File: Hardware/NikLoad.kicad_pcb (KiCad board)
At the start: 2 copper layers, 9 parts, among them Q500 IRFZ24NPbF, Q501 IRFZ24NPbF, Q502 IRFZ24NPbF, Q503 IRFZ24NPbF, Q504 IRFZ24NPbF, Q505 IRFZ24NPbF, Q506 IRFZ24NPbF, Q507 IRFZ24NPbF

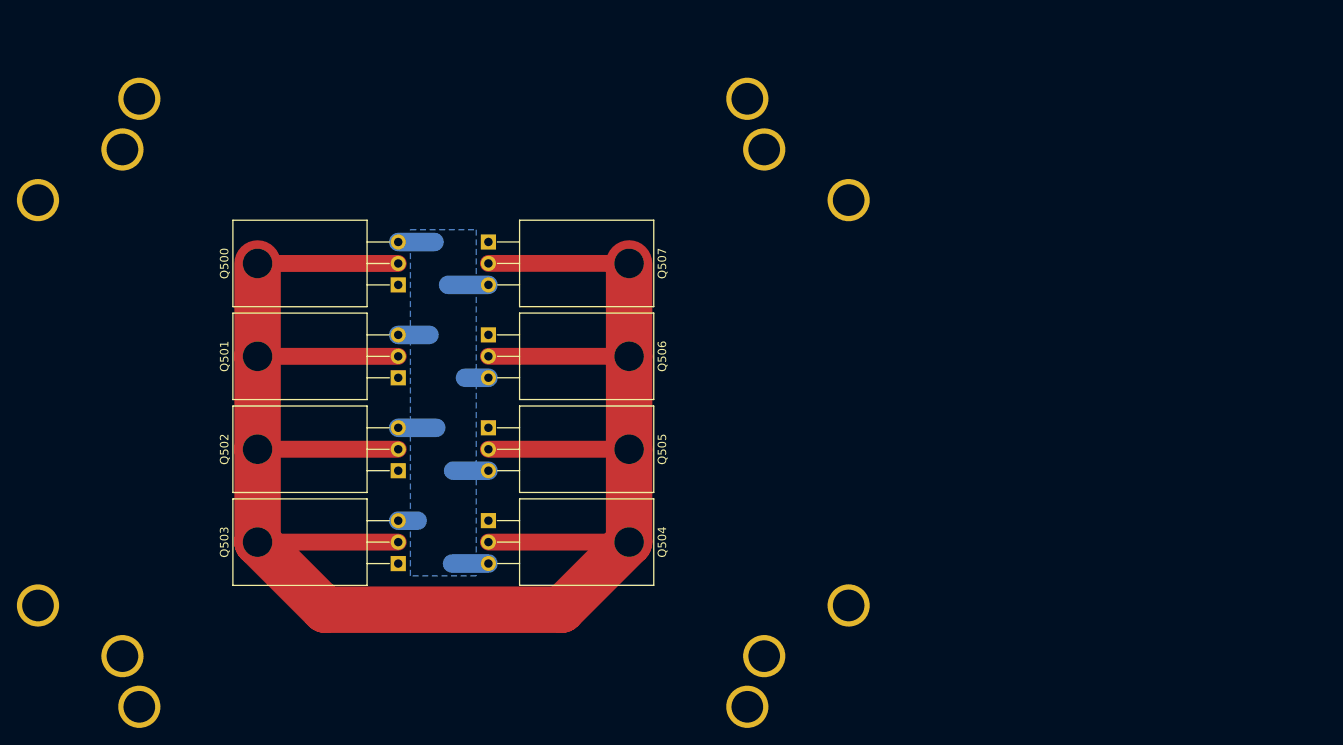
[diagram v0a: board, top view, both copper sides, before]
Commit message: Add current sense
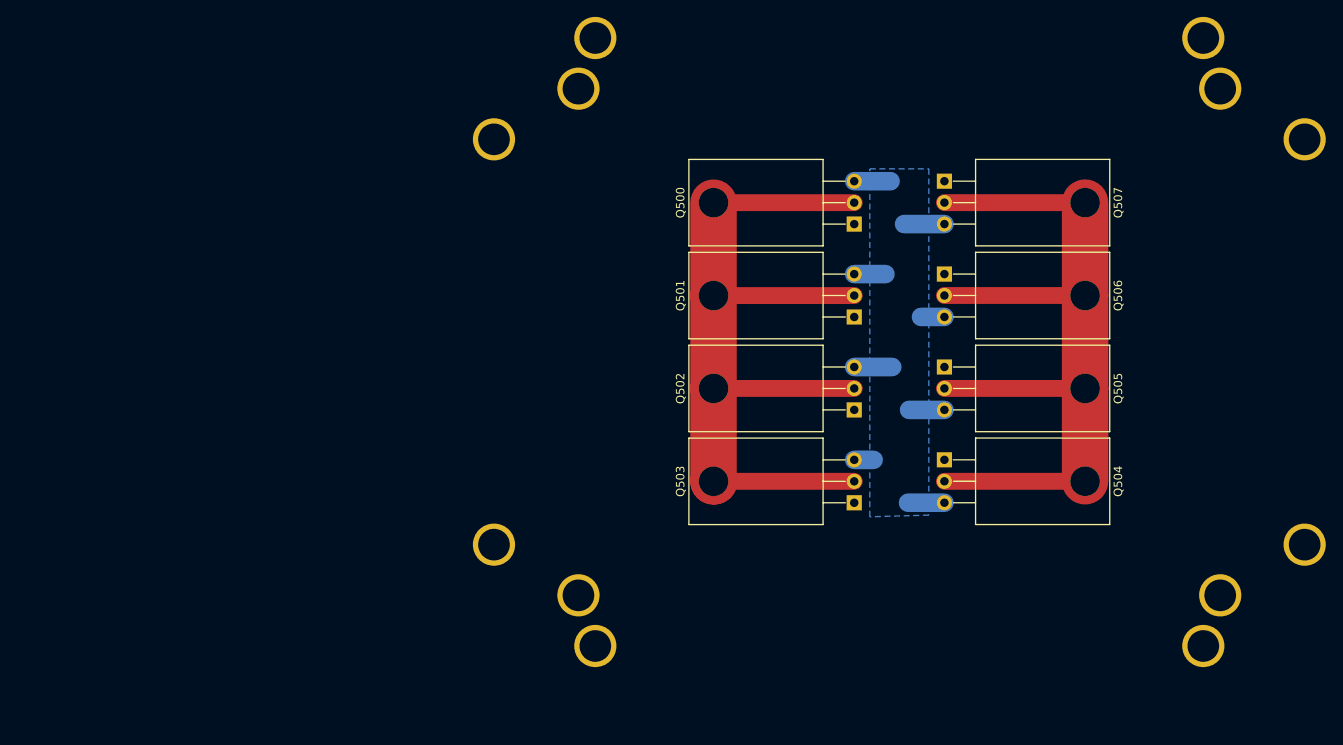
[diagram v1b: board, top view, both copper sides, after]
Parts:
- moved Q500 54.5 mm to (184.2, 77.3)
- moved Q501 54.5 mm to (184.2, 88.3)
- moved Q502 54.5 mm to (184.2, 99.3)
- moved Q503 54.5 mm to (184.2, 110.3)
- moved Q504 54.5 mm to (194.8, 105.3)
- moved Q506 54.5 mm to (194.8, 83.3)
- moved Q507 54.5 mm to (194.8, 72.3)
- moved REF** 54.5 mm to (189.5, 91.3)
- moved Q505 54.5 mm to (194.8, 94.3)
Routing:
- net DUT+: track 250.0 -> 199.4 mm
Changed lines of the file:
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@@
 (kicad_pcb (version 4) (host pcbnew 4.0.7)
   (general
-    (links 22)
-    (no_connects 7)
-    (area 84.8476 59.0726 186.1524 137.1524)
+    (links 0)
+    (no_connects 1)
+    (area 138.8476 51.8726 240.1524 129.9524)
     (thickness 1.6)
     (drawings 0)
-    (tracks 26)
+    (tracks 23)
     (zones 0)
     (modules 9)
@@
   )
   (module pc_cooler_mount:PC_COOLER_MOUNT (layer F.Cu)
-    (at 135.5 98.5)
+    (at 189.5 91.3)
     (fp_text reference REF** (at 19.5 -38.5) (layer F.SilkS) hide
       (effects (font (size 1 1) (thickness 0.15)))
@@
   )
   (module TO-220_plated_mount:TO-220_Horizontal (layer F.Cu)
-    (at 130.16 84.54 90)
+    (at 184.16 77.34 90)
     (descr "TO-220, Horizontal, RM 2.54mm")
     (tags "TO-220 Horizontal RM 2.54mm")
@@
   )
   (module TO-220_plated_mount:TO-220_Horizontal (layer F.Cu)
-    (at 130.16 95.54 90)
+    (at 184.16 88.34 90)
     (descr "TO-220, Horizontal, RM 2.54mm")
     (tags "TO-220 Horizontal RM 2.54mm")
@@
   )
   (module TO-220_plated_mount:TO-220_Horizontal (layer F.Cu)
-    (at 130.16 106.54 90)
+    (at 184.16 99.34 90)
     (descr "TO-220, Horizontal, RM 2.54mm")
     (tags "TO-220 Horizontal RM 2.54mm")
@@
   )
   (module TO-220_plated_mount:TO-220_Horizontal (layer F.Cu)
-    (at 130.16 117.54 90)
+    (at 184.16 110.34 90)
     (descr "TO-220, Horizontal, RM 2.54mm")
     (tags "TO-220 Horizontal RM 2.54mm")
@@
   )
   (module TO-220_plated_mount:TO-220_Horizontal (layer F.Cu)
-    (at 140.84 112.455 270)
+    (at 194.84 105.255 270)
     (descr "TO-220, Horizontal, RM 2.54mm")
     (tags "TO-220 Horizontal RM 2.54mm")
@@
   )
   (module TO-220_plated_mount:TO-220_Horizontal (layer F.Cu)
-    (at 140.84 101.46 270)
+    (at 194.84 94.26 270)
     (descr "TO-220, Horizontal, RM 2.54mm")
     (tags "TO-220 Horizontal RM 2.54mm")
@@
   )
   (module TO-220_plated_mount:TO-220_Horizontal (layer F.Cu)
-    (at 140.84 90.455 270)
+    (at 194.84 83.255 270)
     (descr "TO-220, Horizontal, RM 2.54mm")
     (tags "TO-220 Horizontal RM 2.54mm")
@@
   )
   (module TO-220_plated_mount:TO-220_Horizontal (layer F.Cu)
-    (at 140.84 79.455 270)
+    (at 194.84 72.255 270)
     (descr "TO-220, Horizontal, RM 2.54mm")
     (tags "TO-220 Horizontal RM 2.54mm")
@@
     )
   )
-  (segment (start 149.495 123) (end 121.5 123) (width 5.5) (layer F.Cu) (net 9))
-  (segment (start 121.5 123) (end 113.5 115) (width 5.5) (layer F.Cu) (net 9))
-  (segment (start 149.495 123) (end 157.5 114.995) (width 5.5) (layer F.Cu) (net 9))
-  (segment (start 113.6 115) (end 113.5 115) (width 5.5) (layer F.Cu) (net 9))
-  (segment (start 157.5 92.995) (end 157.5 81.995) (width 5.5) (layer F.Cu) (net 9))
-  (segment (start 157.5 104) (end 157.5 92.995) (width 5.5) (layer F.Cu) (net 9))
-  (segment (start 157.5 114.995) (end 157.5 104) (width 5.5) (layer F.Cu) (net 9))
-  (segment (start 113.5 104) (end 113.5 115) (width 5.5) (layer F.Cu) (net 9))
-  (segment (start 113.5 93) (end 113.5 104) (width 5.5) (layer F.Cu) (net 9))
-  (segment (start 113.5 82) (end 113.5 93) (width 5.5) (layer F.Cu) (net 9))
-  (segment (start 140.84 81.995) (end 157.5 81.995) (width 2) (layer F.Cu) (net 9))
-  (segment (start 140.84 92.995) (end 157.5 92.995) (width 2) (layer F.Cu) (net 9))
-  (segment (start 140.84 104) (end 157.5 104) (width 2) (layer F.Cu) (net 9))
-  (segment (start 140.84 114.995) (end 157.5 114.995) (width 2) (layer F.Cu) (net 9))
-  (segment (start 130.16 115) (end 113.5 115) (width 2) (layer F.Cu) (net 9))
-  (segment (start 130.16 104) (end 113.5 104) (width 2) (layer F.Cu) (net 9))
-  (segment (start 130.16 93) (end 113.5 93) (width 2) (layer F.Cu) (net 9))
-  (segment (start 130.16 82) (end 113.5 82) (width 2) (layer F.Cu) (net 9))
-  (segment (start 140.84 117.535) (end 136.535 117.535) (width 2.2) (layer B.Cu) (net 10))
-  (segment (start 130.16 112.46) (end 132.46 112.46) (width 2.2) (layer B.Cu) (net 10))
-  (segment (start 140.84 106.54) (end 136.66 106.54) (width 2.2) (layer B.Cu) (net 10))
-  (segment (start 130.16 101.46) (end 134.66 101.46) (width 2.2) (layer B.Cu) (net 10))
-  (segment (start 140.84 95.535) (end 138.065 95.535) (width 2.2) (layer B.Cu) (net 10))
-  (segment (start 130.16 90.46) (end 133.86 90.46) (width 2.2) (layer B.Cu) (net 10))
-  (segment (start 140.84 84.535) (end 136.065 84.535) (width 2.2) (layer B.Cu) (net 10))
-  (segment (start 130.16 79.46) (end 134.46 79.46) (width 2.2) (layer B.Cu) (net 10))
+  (segment (start 167.6 107.8) (end 167.5 107.8) (width 5.5) (layer F.Cu) (net 9))
+  (segment (start 211.5 85.795) (end 211.5 74.795) (width 5.5) (layer F.Cu) (net 9))
+  (segment (start 211.5 96.8) (end 211.5 85.795) (width 5.5) (layer F.Cu) (net 9))
+  (segment (start 211.5 107.795) (end 211.5 96.8) (width 5.5) (layer F.Cu) (net 9))
+  (segment (start 167.5 96.8) (end 167.5 107.8) (width 5.5) (layer F.Cu) (net 9))
+  (segment (start 167.5 85.8) (end 167.5 96.8) (width 5.5) (layer F.Cu) (net 9))
+  (segment (start 167.5 74.8) (end 167.5 85.8) (width 5.5) (layer F.Cu) (net 9))
+  (segment (start 194.84 74.795) (end 211.5 74.795) (width 2) (layer F.Cu) (net 9))
+  (segment (start 194.84 85.795) (end 211.5 85.795) (width 2) (layer F.Cu) (net 9))
+  (segment (start 194.84 96.8) (end 211.5 96.8) (width 2) (layer F.Cu) (net 9))
+  (segment (start 194.84 107.795) (end 211.5 107.795) (width 2) (layer F.Cu) (net 9))
+  (segment (start 184.16 107.8) (end 167.5 107.8) (width 2) (layer F.Cu) (net 9))
+  (segment (start 184.16 96.8) (end 167.5 96.8) (width 2) (layer F.Cu) (net 9))
+  (segment (start 184.16 85.8) (end 167.5 85.8) (width 2) (layer F.Cu) (net 9))
+  (segment (start 184.16 74.8) (end 167.5 74.8) (width 2) (layer F.Cu) (net 9))
+  (segment (start 194.84 110.335) (end 190.535 110.335) (width 2.2) (layer B.Cu) (net 10))
+  (segment (start 184.16 105.26) (end 186.46 105.26) (width 2.2) (layer B.Cu) (net 10))
+  (segment (start 194.84 99.34) (end 190.66 99.34) (width 2.2) (layer B.Cu) (net 10))
+  (segment (start 184.16 94.26) (end 188.66 94.26) (width 2.2) (layer B.Cu) (net 10))
+  (segment (start 194.84 88.335) (end 192.065 88.335) (width 2.2) (layer B.Cu) (net 10))
+  (segment (start 184.16 83.26) (end 187.86 83.26) (width 2.2) (layer B.Cu) (net 10))
+  (segment (start 194.84 77.335) (end 190.065 77.335) (width 2.2) (layer B.Cu) (net 10))
+  (segment (start 184.16 72.26) (end 188.46 72.26) (width 2.2) (layer B.Cu) (net 10))
   (zone (net 10) (net_name CURRENT_SENSE+) (layer B.Cu) (hatch edge 0.508)
     (priority 10)
@@
     (polygon
       (pts
-        (xy 131.6 78) (xy 139.4 78) (xy 139.4 119) (xy 131.6 119)
+        (xy 186 70.8) (xy 193 70.8) (xy 193 111.8) (xy 186 112)
       )
     )
   )
-  (zone (net 10) (net_name CURRENT_SENSE+) (layer F.Mask) (hatch edge 0.508)
+  (zone (net 0) (net_name "") (layer F.Mask) (hatch edge 0.508)
     (priority 10)
     (connect_pads (clearance 0.508))
@@
     (polygon
       (pts
-        (xy 116.2 117.4) (xy 116.2 79.2) (xy 110.6 79.2) (xy 110.6 117.4)
+        (xy 170.2 110.2) (xy 170.2 72) (xy 164.6 72) (xy 164.6 110.2)
       )
     )
   )
-  (zone (net 10) (net_name CURRENT_SENSE+) (layer F.Mask) (hatch edge 0.508)
+  (zone (net 0) (net_name "") (layer F.Mask) (hatch edge 0.508)
     (priority 10)
     (connect_pads (clearance 0.508))
@@
     (polygon
       (pts
-        (xy 160.322941 117.4) (xy 160.322941 79.2) (xy 154.722941 79.2) (xy 154.722941 117.4)
+        (xy 214.322941 110.2) (xy 214.322941 72) (xy 208.722941 72) (xy 208.722941 110.2)
       )
     )

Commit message: Preliminary measurement setup
Deleted net file, not yet needed.
Added preliminary measurement stuff.
Still need DAC for the offset voltage, and need to find a new ADC.
Also, doing isolation. Analog board will have +12V in, isolate power on board.
Isolated 2 channels of SPI between digital and analog.
Also, add a bunch of files I forgot to add to git. Oops.
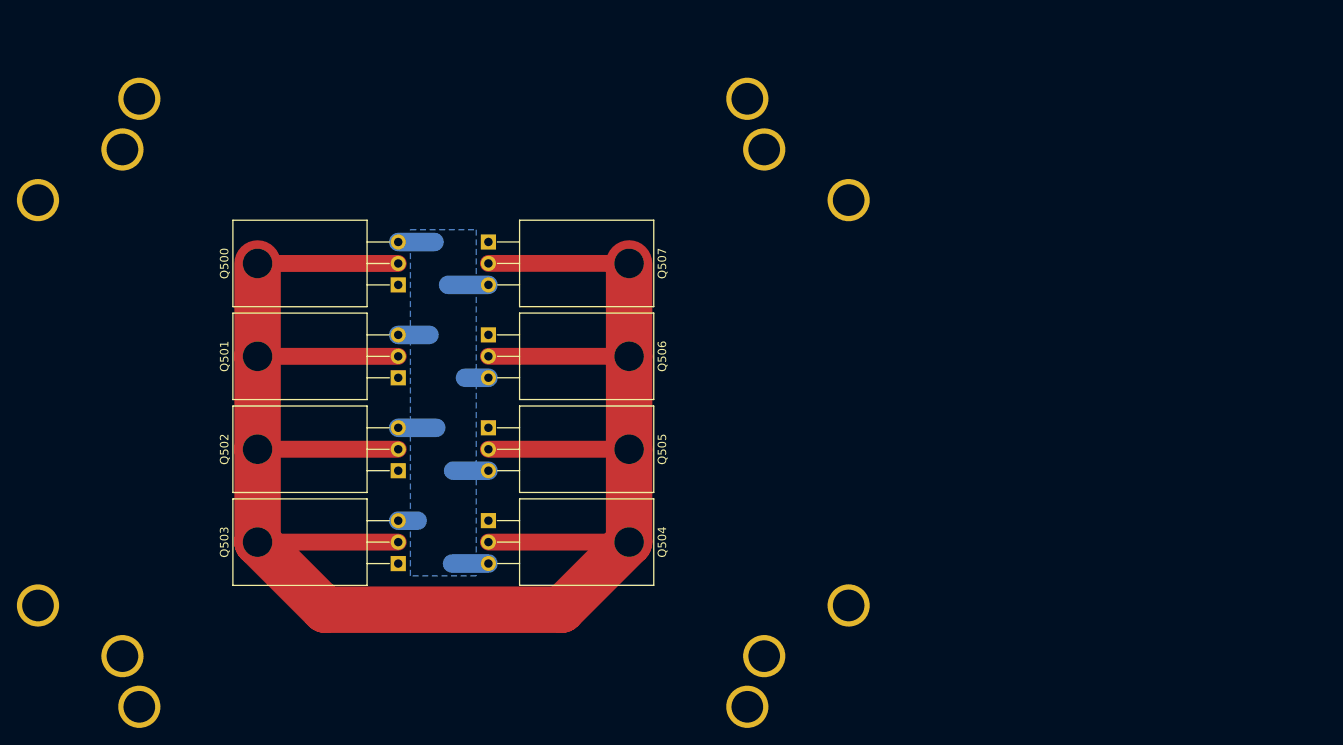
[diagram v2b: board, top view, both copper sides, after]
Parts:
- moved Q500 54.5 mm to (130.2, 84.5)
- moved Q501 54.5 mm to (130.2, 95.5)
- moved Q502 54.5 mm to (130.2, 106.5)
- moved Q503 54.5 mm to (130.2, 117.5)
- moved Q504 54.5 mm to (140.8, 112.5)
- moved Q506 54.5 mm to (140.8, 90.5)
- moved Q507 54.5 mm to (140.8, 79.5)
- moved REF** 54.5 mm to (135.5, 98.5)
- moved Q505 54.5 mm to (140.8, 101.5)
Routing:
- net DUT+: track 199.4 -> 250.0 mm
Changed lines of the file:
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@@
 (kicad_pcb (version 4) (host pcbnew 4.0.7)
   (general
-    (links 0)
-    (no_connects 1)
-    (area 138.8476 51.8726 240.1524 129.9524)
+    (links 22)
+    (no_connects 7)
+    (area 84.8476 59.0726 186.1524 137.1524)
     (thickness 1.6)
     (drawings 0)
-    (tracks 23)
+    (tracks 26)
     (zones 0)
     (modules 9)
@@
   )
   (module pc_cooler_mount:PC_COOLER_MOUNT (layer F.Cu)
-    (at 189.5 91.3)
+    (at 135.5 98.5)
     (fp_text reference REF** (at 19.5 -38.5) (layer F.SilkS) hide
       (effects (font (size 1 1) (thickness 0.15)))
@@
   )
   (module TO-220_plated_mount:TO-220_Horizontal (layer F.Cu)
-    (at 184.16 77.34 90)
+    (at 130.16 84.54 90)
     (descr "TO-220, Horizontal, RM 2.54mm")
     (tags "TO-220 Horizontal RM 2.54mm")
@@
   )
   (module TO-220_plated_mount:TO-220_Horizontal (layer F.Cu)
-    (at 184.16 88.34 90)
+    (at 130.16 95.54 90)
     (descr "TO-220, Horizontal, RM 2.54mm")
     (tags "TO-220 Horizontal RM 2.54mm")
@@
   )
   (module TO-220_plated_mount:TO-220_Horizontal (layer F.Cu)
-    (at 184.16 99.34 90)
+    (at 130.16 106.54 90)
     (descr "TO-220, Horizontal, RM 2.54mm")
     (tags "TO-220 Horizontal RM 2.54mm")
@@
   )
   (module TO-220_plated_mount:TO-220_Horizontal (layer F.Cu)
-    (at 184.16 110.34 90)
+    (at 130.16 117.54 90)
     (descr "TO-220, Horizontal, RM 2.54mm")
     (tags "TO-220 Horizontal RM 2.54mm")
@@
   )
   (module TO-220_plated_mount:TO-220_Horizontal (layer F.Cu)
-    (at 194.84 105.255 270)
+    (at 140.84 112.455 270)
     (descr "TO-220, Horizontal, RM 2.54mm")
     (tags "TO-220 Horizontal RM 2.54mm")
@@
   )
   (module TO-220_plated_mount:TO-220_Horizontal (layer F.Cu)
-    (at 194.84 94.26 270)
+    (at 140.84 101.46 270)
     (descr "TO-220, Horizontal, RM 2.54mm")
     (tags "TO-220 Horizontal RM 2.54mm")
@@
   )
   (module TO-220_plated_mount:TO-220_Horizontal (layer F.Cu)
-    (at 194.84 83.255 270)
+    (at 140.84 90.455 270)
     (descr "TO-220, Horizontal, RM 2.54mm")
     (tags "TO-220 Horizontal RM 2.54mm")
@@
   )
   (module TO-220_plated_mount:TO-220_Horizontal (layer F.Cu)
-    (at 194.84 72.255 270)
+    (at 140.84 79.455 270)
     (descr "TO-220, Horizontal, RM 2.54mm")
     (tags "TO-220 Horizontal RM 2.54mm")
@@
     )
   )
-  (segment (start 167.6 107.8) (end 167.5 107.8) (width 5.5) (layer F.Cu) (net 9))
-  (segment (start 211.5 85.795) (end 211.5 74.795) (width 5.5) (layer F.Cu) (net 9))
-  (segment (start 211.5 96.8) (end 211.5 85.795) (width 5.5) (layer F.Cu) (net 9))
-  (segment (start 211.5 107.795) (end 211.5 96.8) (width 5.5) (layer F.Cu) (net 9))
-  (segment (start 167.5 96.8) (end 167.5 107.8) (width 5.5) (layer F.Cu) (net 9))
-  (segment (start 167.5 85.8) (end 167.5 96.8) (width 5.5) (layer F.Cu) (net 9))
-  (segment (start 167.5 74.8) (end 167.5 85.8) (width 5.5) (layer F.Cu) (net 9))
-  (segment (start 194.84 74.795) (end 211.5 74.795) (width 2) (layer F.Cu) (net 9))
-  (segment (start 194.84 85.795) (end 211.5 85.795) (width 2) (layer F.Cu) (net 9))
-  (segment (start 194.84 96.8) (end 211.5 96.8) (width 2) (layer F.Cu) (net 9))
-  (segment (start 194.84 107.795) (end 211.5 107.795) (width 2) (layer F.Cu) (net 9))
-  (segment (start 184.16 107.8) (end 167.5 107.8) (width 2) (layer F.Cu) (net 9))
-  (segment (start 184.16 96.8) (end 167.5 96.8) (width 2) (layer F.Cu) (net 9))
-  (segment (start 184.16 85.8) (end 167.5 85.8) (width 2) (layer F.Cu) (net 9))
-  (segment (start 184.16 74.8) (end 167.5 74.8) (width 2) (layer F.Cu) (net 9))
-  (segment (start 194.84 110.335) (end 190.535 110.335) (width 2.2) (layer B.Cu) (net 10))
-  (segment (start 184.16 105.26) (end 186.46 105.26) (width 2.2) (layer B.Cu) (net 10))
-  (segment (start 194.84 99.34) (end 190.66 99.34) (width 2.2) (layer B.Cu) (net 10))
-  (segment (start 184.16 94.26) (end 188.66 94.26) (width 2.2) (layer B.Cu) (net 10))
-  (segment (start 194.84 88.335) (end 192.065 88.335) (width 2.2) (layer B.Cu) (net 10))
-  (segment (start 184.16 83.26) (end 187.86 83.26) (width 2.2) (layer B.Cu) (net 10))
-  (segment (start 194.84 77.335) (end 190.065 77.335) (width 2.2) (layer B.Cu) (net 10))
-  (segment (start 184.16 72.26) (end 188.46 72.26) (width 2.2) (layer B.Cu) (net 10))
+  (segment (start 149.495 123) (end 121.5 123) (width 5.5) (layer F.Cu) (net 9))
+  (segment (start 121.5 123) (end 113.5 115) (width 5.5) (layer F.Cu) (net 9))
+  (segment (start 149.495 123) (end 157.5 114.995) (width 5.5) (layer F.Cu) (net 9))
+  (segment (start 113.6 115) (end 113.5 115) (width 5.5) (layer F.Cu) (net 9))
+  (segment (start 157.5 92.995) (end 157.5 81.995) (width 5.5) (layer F.Cu) (net 9))
+  (segment (start 157.5 104) (end 157.5 92.995) (width 5.5) (layer F.Cu) (net 9))
+  (segment (start 157.5 114.995) (end 157.5 104) (width 5.5) (layer F.Cu) (net 9))
+  (segment (start 113.5 104) (end 113.5 115) (width 5.5) (layer F.Cu) (net 9))
+  (segment (start 113.5 93) (end 113.5 104) (width 5.5) (layer F.Cu) (net 9))
+  (segment (start 113.5 82) (end 113.5 93) (width 5.5) (layer F.Cu) (net 9))
+  (segment (start 140.84 81.995) (end 157.5 81.995) (width 2) (layer F.Cu) (net 9))
+  (segment (start 140.84 92.995) (end 157.5 92.995) (width 2) (layer F.Cu) (net 9))
+  (segment (start 140.84 104) (end 157.5 104) (width 2) (layer F.Cu) (net 9))
+  (segment (start 140.84 114.995) (end 157.5 114.995) (width 2) (layer F.Cu) (net 9))
+  (segment (start 130.16 115) (end 113.5 115) (width 2) (layer F.Cu) (net 9))
+  (segment (start 130.16 104) (end 113.5 104) (width 2) (layer F.Cu) (net 9))
+  (segment (start 130.16 93) (end 113.5 93) (width 2) (layer F.Cu) (net 9))
+  (segment (start 130.16 82) (end 113.5 82) (width 2) (layer F.Cu) (net 9))
+  (segment (start 140.84 117.535) (end 136.535 117.535) (width 2.2) (layer B.Cu) (net 10))
+  (segment (start 130.16 112.46) (end 132.46 112.46) (width 2.2) (layer B.Cu) (net 10))
+  (segment (start 140.84 106.54) (end 136.66 106.54) (width 2.2) (layer B.Cu) (net 10))
+  (segment (start 130.16 101.46) (end 134.66 101.46) (width 2.2) (layer B.Cu) (net 10))
+  (segment (start 140.84 95.535) (end 138.065 95.535) (width 2.2) (layer B.Cu) (net 10))
+  (segment (start 130.16 90.46) (end 133.86 90.46) (width 2.2) (layer B.Cu) (net 10))
+  (segment (start 140.84 84.535) (end 136.065 84.535) (width 2.2) (layer B.Cu) (net 10))
+  (segment (start 130.16 79.46) (end 134.46 79.46) (width 2.2) (layer B.Cu) (net 10))
   (zone (net 10) (net_name CURRENT_SENSE+) (layer B.Cu) (hatch edge 0.508)
     (priority 10)
@@
     (polygon
       (pts
-        (xy 186 70.8) (xy 193 70.8) (xy 193 111.8) (xy 186 112)
+        (xy 131.6 78) (xy 139.4 78) (xy 139.4 119) (xy 131.6 119)
       )
     )
   )
-  (zone (net 0) (net_name "") (layer F.Mask) (hatch edge 0.508)
+  (zone (net 10) (net_name CURRENT_SENSE+) (layer F.Mask) (hatch edge 0.508)
     (priority 10)
     (connect_pads (clearance 0.508))
@@
     (polygon
       (pts
-        (xy 170.2 110.2) (xy 170.2 72) (xy 164.6 72) (xy 164.6 110.2)
+        (xy 116.2 117.4) (xy 116.2 79.2) (xy 110.6 79.2) (xy 110.6 117.4)
       )
     )
   )
-  (zone (net 0) (net_name "") (layer F.Mask) (hatch edge 0.508)
+  (zone (net 10) (net_name CURRENT_SENSE+) (layer F.Mask) (hatch edge 0.508)
     (priority 10)
     (connect_pads (clearance 0.508))
@@
     (polygon
       (pts
-        (xy 214.322941 110.2) (xy 214.322941 72) (xy 208.722941 72) (xy 208.722941 110.2)
+        (xy 160.322941 117.4) (xy 160.322941 79.2) (xy 154.722941 79.2) (xy 154.722941 117.4)
       )
     )
